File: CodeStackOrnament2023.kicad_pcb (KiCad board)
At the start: 2 copper layers, 28 parts, among them SW1 SW_SPST, U1 TLC555xD, U2 74VHC4040FT

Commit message: starting board design
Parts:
- removed C8: 10uf, Capacitor_SMD:C_0805_2012Metric
- removed the D1 at (117.3, 92.1)
- removed R3: 0, Resistor_SMD:R_0805_2012Metric
- added D1: LED_Small, CodeStackOrnament2023Footprints:156120RS75300_LED, F.Cu at (178.2, 89.0)
- added D1: LED_Small, CodeStackOrnament2023Footprints:156120RS75300_LED, F.Cu at (182.2, 105.1)
- added D1: LED_Small, CodeStackOrnament2023Footprints:156120RS75300_LED, F.Cu at (165.6, 132.8)
- added D1: LED_Small, CodeStackOrnament2023Footprints:156120RS75300_LED, F.Cu at (134.4, 76.4)
- added D1: LED_Small, CodeStackOrnament2023Footprints:156120RS75300_LED, F.Cu at (149.5, 136.8)
- added D1: LED_Small, CodeStackOrnament2023Footprints:156120RS75300_LED, F.Cu at (150.5, 72.4)
- added D1: LED_Small, CodeStackOrnament2023Footprints:156120RS75300_LED, F.Cu at (122.4, 88.0)
- added D1: LED_Small, CodeStackOrnament2023Footprints:156120RS75300_LED, F.Cu at (121.8, 120.2)
- added D1: LED_Small, CodeStackOrnament2023Footprints:156120RS75300_LED, F.Cu at (117.8, 104.1)
- added D1: LED_Small, CodeStackOrnament2023Footprints:156120RS75300_LED, F.Cu at (166.6, 77.0)
- added D1: LED_Small, CodeStackOrnament2023Footprints:156120RS75300_LED, F.Cu at (133.4, 132.2)
- added D1: LED_Small, CodeStackOrnament2023Footprints:156120RS75300_LED, F.Cu at (177.6, 121.2)
- BT1: footprint CodeStackOrnament2023Footprints:2466_AAA_HOLDER -> CodeStackOrnament2023Footprints:BAT_2468
- C1: value c=C_Polarized_Small -> 10uF
- C5: value 0.01uF -> 0.1u
- C7: value 0.1u -> 10uf
- R1, R2: value R -> 8k
- U1: footprint Package_SO:SOIC-8_3.9x4.9mm_P1.27mm -> CodeStackOrnament2023Footprints:TLC555_SOIC
- moved C1 135.7 mm to (247.6, 71.6)
- moved C2 135.7 mm to (247.6, 74.6)
- moved C3 135.7 mm to (247.6, 77.6)
- moved C4 135.7 mm to (247.6, 80.6)
- moved C5 135.7 mm to (247.6, 83.7)
- moved C6 135.7 mm to (247.6, 86.7)
- moved C7 135.7 mm to (247.6, 89.7)
- moved D11 114.3 mm to (213.0, 20.8)
- moved D2 108.8 mm to (211.5, 40.7)
- moved D3 108.8 mm to (211.5, 43.8)
- moved D4 108.8 mm to (211.5, 46.9)
- moved D10 106.5 mm to (212.1, 28.5)
- moved D5 97.9 mm to (211.5, 50.0)
- moved D7 97.9 mm to (211.5, 56.2)
- moved D6 97.9 mm to (211.5, 53.1)
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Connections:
- SW1 pad 1: Net-(BT1-+) -> (no net)
- SW1 pad 2: Net-(SW1-B) -> Net-(BT1-+)
- SW1 pad 3: (no net) -> Net-(SW1-B)
- U2 pad 10: Net-(U2-CLK) -> Net-(U1-Q)
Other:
- board outline added: 68.8 x 68.8 mm

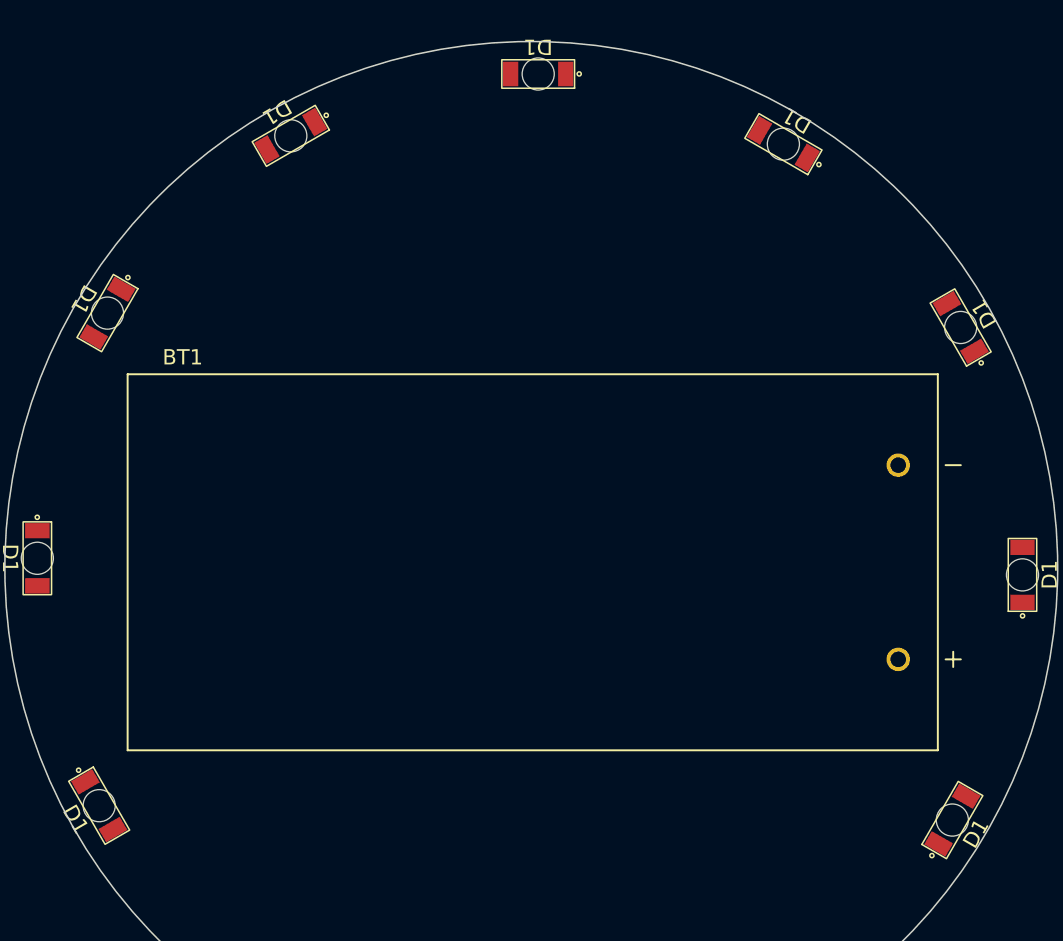
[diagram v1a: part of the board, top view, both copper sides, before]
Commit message: updating footprints
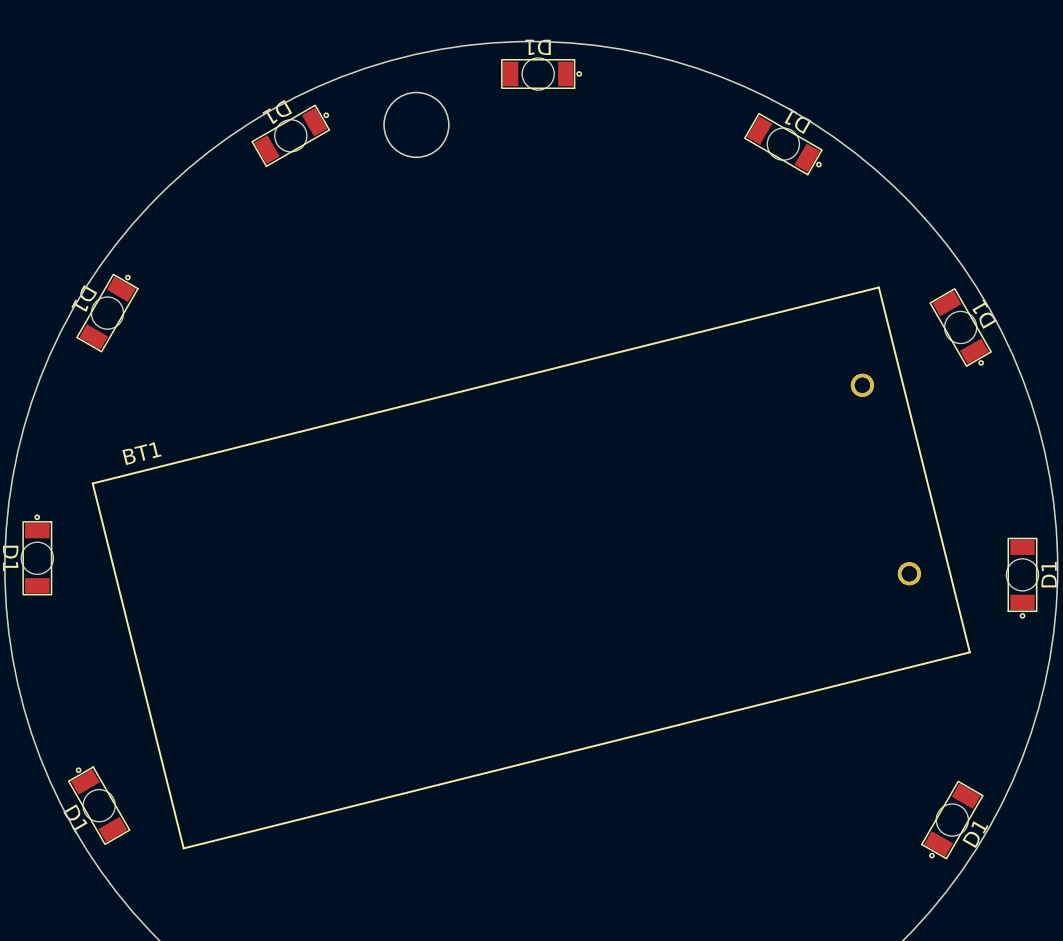
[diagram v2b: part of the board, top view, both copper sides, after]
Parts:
- moved BT1 0.38 mm to (150.1, 104.7), turned to 14 degrees
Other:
- outline, holes or cut-outs redrawn
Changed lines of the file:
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@@
+    )
+  )
+  (footprint "CodeStackOrnament2023Footprints:BAT_2468" (layer "F.Cu")
+    (at 150.09 104.688605 14)
+    (property "Sheetfile" "CodeStackOrnament2023.kicad_sch")
+    (property "Sheetname" "")
+    (property "Sim.Device" "V")
+    (property "Sim.Params" "dc=\"\"")
+    (property "Sim.Pins" "1=+ 2=-")
+    (property "Sim.Type" "DC")
+    (property "ki_description" "Single-cell battery")
+    (property "ki_keywords" "battery cell")
+    (attr through_hole)
+    (fp_text reference "BT1" (at -22.89 -13.4 14) (layer "F.SilkS")
+        (effects (font (size 1 1) (thickness 0.15)))
+    )
+    (fp_text value "Battery_Cell" (at -20.985 13.4 14) (layer "F.Fab")
+        (effects (font (size 1 1) (thickness 0.15)))
+    )
+    (fp_line (start -26.49 -12.295) (end 26.49 -12.295)
+      (stroke (width 0.127) (type solid)) (layer "F.SilkS"))
+    (fp_line (start -26.49 12.295) (end -26.49 -12.295)
+      (stroke (width 0.127) (type solid)) (layer "F.SilkS"))
+    (fp_line (start 26.49 -12.295) (end 26.49 12.295)
+      (stroke (width 0.127) (type solid)) (layer "F.SilkS"))
+    (fp_line (start 26.49 12.295) (end -26.49 12.295)
+      (stroke (width 0.127) (type solid)) (layer "F.SilkS"))
+    (fp_line (start -26.74 -12.545) (end 26.74 -12.545)
+      (stroke (width 0.05) (type solid)) (layer "F.CrtYd"))
+    (fp_line (start -26.74 12.545) (end -26.74 -12.545)
+      (stroke (width 0.05) (type solid)) (layer "F.CrtYd"))
+    (fp_line (start 26.74 -12.545) (end 26.74 12.545)
+      (stroke (width 0.05) (type solid)) (layer "F.CrtYd"))
+    (fp_line (start 26.74 12.545) (end -26.74 12.545)
+      (stroke (width 0.05) (type solid)) (layer "F.CrtYd"))
+    (fp_line (start -26.49 -12.295) (end 26.49 -12.295)
+      (stroke (width 0.127) (type solid)) (layer "F.Fab"))
+    (fp_line (start -26.49 12.295) (end -26.49 -12.295)
+      (stroke (width 0.127) (type solid)) (layer "F.Fab"))
+    (fp_line (start 26.49 -12.295) (end 26.49 12.295)
+      (stroke (width 0.127) (type solid)) (layer "F.Fab"))
+    (fp_line (start 26.49 12.295) (end -26.49 12.295)
+      (stroke (width 0.127) (type solid)) (layer "F.Fab"))
+    (pad "1" thru_hole circle (at 23.9 6.35 14) (size 1.53 1.53) (drill 1.02) (layers "*.Cu" "*.Mask")
+      (net 1 "Net-(BT1-+)") (pinfunction "+") (pintype "passive") (solder_mask_margin 0.102))
+    (pad "2" thru_hole circle (at 23.9 -6.35 14) (size 1.53 1.53) (drill 1.02) (layers "*.Cu" "*.Mask")
+      (net 2 "GND") (pinfunction "-") (pintype "passive") (solder_mask_margin 0.102))
+    (model "${KIPRJMOD}/lib/2468.step"
+      (offset (xyz -6.5 -1.5 10))
+      (scale (xyz 1 1 1))
+      (rotate (xyz -90 0 0))
     )
   )
@@
     )
   )
-  (footprint "CodeStackOrnament2023Footprints:BAT_2468" (layer "F.Cu")
-    (at 150.184645 104.318605)
-    (property "Sheetfile" "CodeStackOrnament2023.kicad_sch")
-    (property "Sheetname" "")
-    (property "Sim.Device" "V")
-    (property "Sim.Params" "dc=\"\"")
-    (property "Sim.Pins" "1=+ 2=-")
-    (property "Sim.Type" "DC")
-    (property "ki_description" "Single-cell battery")
-    (property "ki_keywords" "battery cell")
-    (attr through_hole)
-    (fp_text reference "BT1" (at -22.89 -13.4) (layer "F.SilkS")
-        (effects (font (size 1 1) (thickness 0.15)))
-    )
-    (fp_text value "Battery_Cell" (at -20.985 13.4) (layer "F.Fab")
-        (effects (font (size 1 1) (thickness 0.15)))
-    )
-    (fp_line (start -26.49 -12.295) (end 26.49 -12.295)
-      (stroke (width 0.127) (type solid)) (layer "F.SilkS"))
-    (fp_line (start -26.49 12.295) (end -26.49 -12.295)
-      (stroke (width 0.127) (type solid)) (layer "F.SilkS"))
-    (fp_line (start 26.49 -12.295) (end 26.49 12.295)
-      (stroke (width 0.127) (type solid)) (layer "F.SilkS"))
-    (fp_line (start 26.49 12.295) (end -26.49 12.295)
-      (stroke (width 0.127) (type solid)) (layer "F.SilkS"))
-    (fp_line (start 26.995 -6.35) (end 27.995 -6.35)
-      (stroke (width 0.127) (type solid)) (layer "F.SilkS"))
-    (fp_line (start 26.995 6.35) (end 27.995 6.35)
-      (stroke (width 0.127) (type solid)) (layer "F.SilkS"))
-    (fp_line (start 27.495 5.85) (end 27.495 6.85)
-      (stroke (width 0.127) (type solid)) (layer "F.SilkS"))
-    (fp_line (start -26.74 -12.545) (end 26.74 -12.545)
-      (stroke (width 0.05) (type solid)) (layer "F.CrtYd"))
-    (fp_line (start -26.74 12.545) (end -26.74 -12.545)
-      (stroke (width 0.05) (type solid)) (layer "F.CrtYd"))
-    (fp_line (start 26.74 -12.545) (end 26.74 12.545)
-      (stroke (width 0.05) (type solid)) (layer "F.CrtYd"))
-    (fp_line (start 26.74 12.545) (end -26.74 12.545)
-      (stroke (width 0.05) (type solid)) (layer "F.CrtYd"))
-    (fp_line (start -26.49 -12.295) (end 26.49 -12.295)
-      (stroke (width 0.127) (type solid)) (layer "F.Fab"))
-    (fp_line (start -26.49 12.295) (end -26.49 -12.295)
-      (stroke (width 0.127) (type solid)) (layer "F.Fab"))
-    (fp_line (start 26.49 -12.295) (end 26.49 12.295)
-      (stroke (width 0.127) (type solid)) (layer "F.Fab"))
-    (fp_line (start 26.49 12.295) (end -26.49 12.295)
-      (stroke (width 0.127) (type solid)) (layer "F.Fab"))
-    (fp_line (start 26.995 -6.35) (end 27.995 -6.35)
-      (stroke (width 0.127) (type solid)) (layer "F.Fab"))
-    (fp_line (start 26.995 6.35) (end 27.995 6.35)
-      (stroke (width 0.127) (type solid)) (layer "F.Fab"))
-    (fp_line (start 27.495 5.85) (end 27.495 6.85)
-      (stroke (width 0.127) (type solid)) (layer "F.Fab"))
-    (pad "1" thru_hole circle (at 23.9 6.35) (size 1.53 1.53) (drill 1.02) (layers "*.Cu" "*.Mask")
-      (net 1 "Net-(BT1-+)") (pinfunction "+") (pintype "passive") (solder_mask_margin 0.102))
-    (pad "2" thru_hole circle (at 23.9 -6.35) (size 1.53 1.53) (drill 1.02) (layers "*.Cu" "*.Mask")
-      (net 2 "GND") (pinfunction "-") (pintype "passive") (solder_mask_margin 0.102))
-    (model "${KIPRJMOD}/lib/2468.step"
-      (offset (xyz -6.5 -1.5 10))
-      (scale (xyz 1 1 1))
-      (rotate (xyz -90 0 0))
-    )
-  )
   (footprint "CodeStackOrnament2023Footprints:156120RS75300_LED" (layer "F.Cu")
     (at 134.36502 76.433956 -150)
@@
     )
   )
+  (gr_circle (center 142.58 75.72) (end 144.59 76.39)
+    (stroke (width 0.1) (type default)) (fill none) (layer "Edge.Cuts"))
   (gr_circle (center 150.09 104.688605) (end 170.99 132.038605)
     (stroke (width 0.1) (type default)) (fill none) (layer "Edge.Cuts"))

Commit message: board layout
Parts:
- F1: footprint Resistor_SMD:R_0805_2012Metric -> CodeStackOrnament2023Footprints:SMD1206B050TF_FUSE
- moved C2 115.9 mm to (144.3, 127.3), turned to 90 degrees
- moved C1 115.6 mm to (144.4, 123.7), turned to 90 degrees
- moved C5 112.7 mm to (141.2, 120.8)
- moved C3 112.2 mm to (148.0, 129.3)
- moved C4 107.4 mm to (151.8, 129.3), turned to 180 degrees
- moved U2 99.1 mm to (137.4, 124.9)
- moved C7 96.3 mm to (158.1, 125.3), turned to -90 degrees
- moved C6 95.5 mm to (160.3, 125.3), turned to -90 degrees
- moved U1 81.7 mm to (147.4, 123.3)
- moved SW1 62.1 mm to (166.0, 124.3), turned to -90 degrees
- moved R2 60.9 mm to (154.9, 127.0), turned to -90 degrees
- moved R1 60.5 mm to (154.9, 123.3), turned to -90 degrees
- moved F1 33.1 mm to (178.9, 106.1), turned to 90 degrees
- moved D1 7.88 mm to (127.2, 81.8), turned to -134 degrees
- moved D1 7.88 mm to (141.7, 73.5), turned to -164 degrees
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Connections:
- F1 pad 1: +3V0 -> Net-(SW1-A)
- F1 pad 2: Net-(SW1-B) -> Net-(BT1-+)
- SW1 pad 2: Net-(BT1-+) -> Net-(SW1-A)
- SW1 pad 3: Net-(SW1-B) -> +3V0
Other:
- outline, holes or cut-outs redrawn

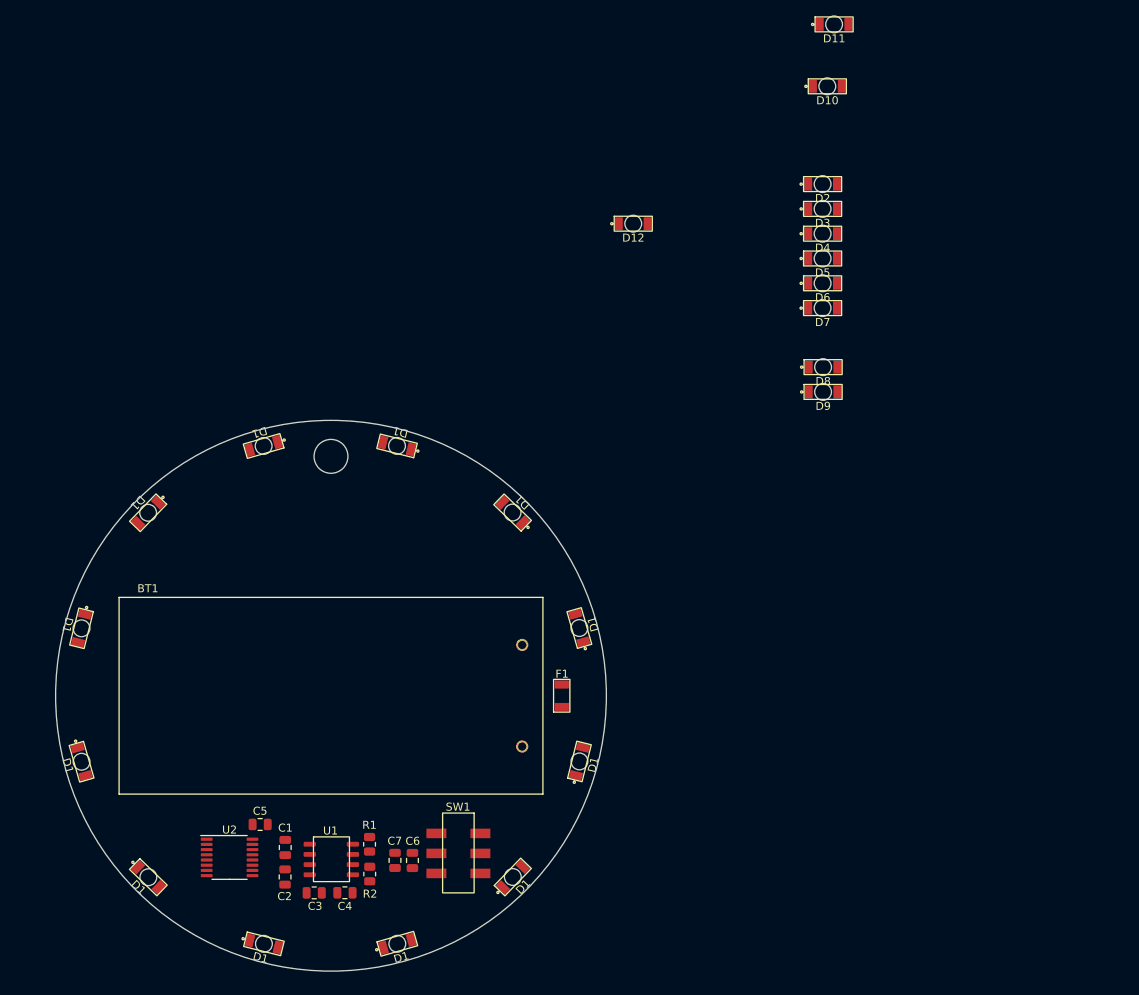
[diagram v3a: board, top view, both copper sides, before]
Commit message: starting board routing
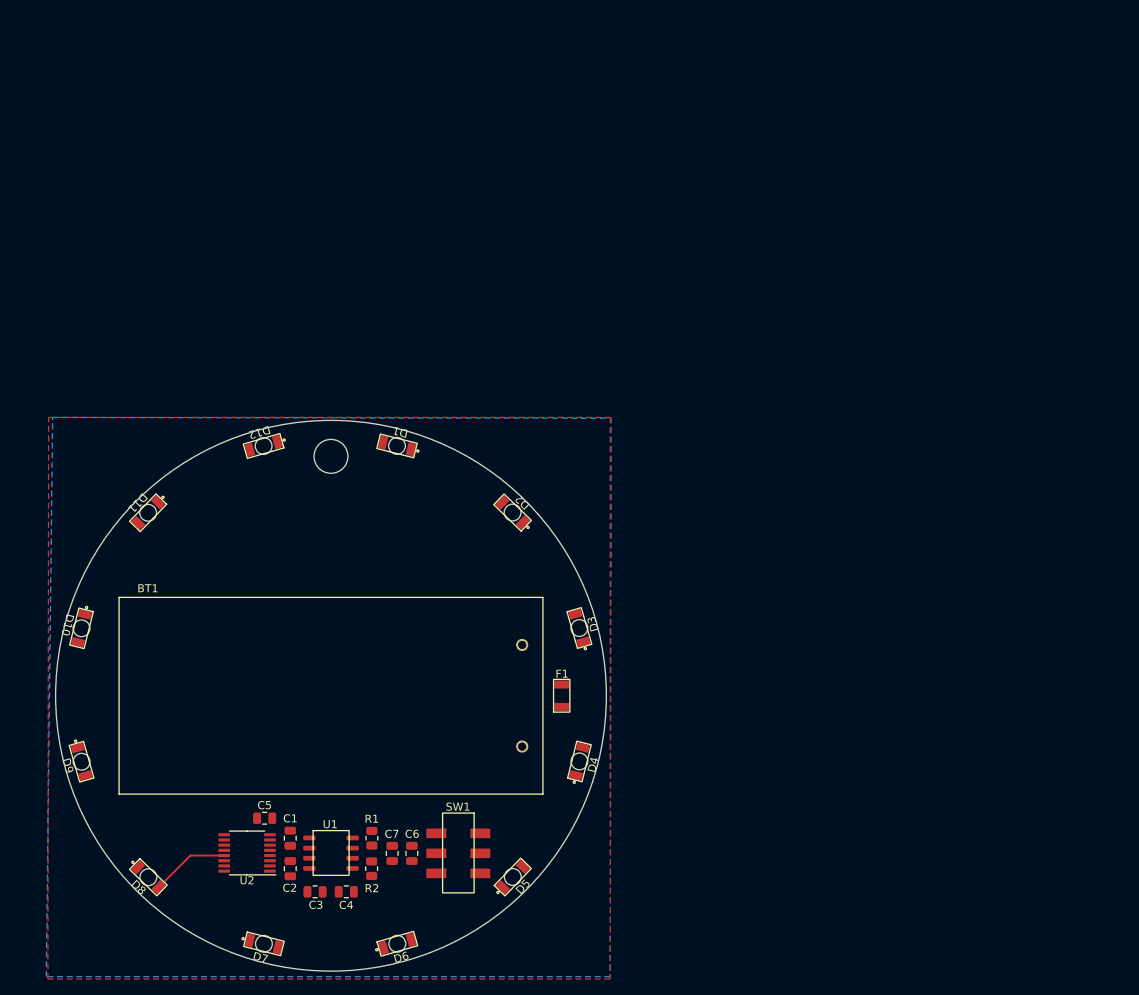
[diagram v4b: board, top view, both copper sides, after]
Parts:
- removed the D10 at (212.1, 28.5)
- removed the D11 at (213.0, 20.8)
- removed the D12 at (187.9, 45.7)
- removed the D2 at (211.5, 40.7)
- removed the D3 at (211.5, 43.8)
- removed the D4 at (211.5, 46.9)
- removed the D5 at (211.5, 50.0)
- removed the D6 at (211.5, 53.1)
- removed the D7 at (211.5, 56.2)
- removed the D8 at (211.6, 63.6)
- removed the D9 at (211.6, 66.7)
- moved U2 2.26 mm to (139.6, 124.3), turned to 180 degrees
- moved C1 1.32 mm to (145.0, 122.5)
- moved C2 1.23 mm to (145.0, 126.3)
- moved C5 0.97 mm to (141.8, 120.0), turned to 180 degrees
- moved C7 0.94 mm to (157.7, 124.4)
- moved C6 0.88 mm to (160.2, 124.4)
- moved R1 0.81 mm to (155.2, 122.5)
- moved U1 0.79 mm to (147.4, 122.5)
- moved R2 0.72 mm to (155.2, 126.3)
- moved C4 0.21 mm to (152.0, 129.2)
- moved C3 0.17 mm to (148.1, 129.2)
- renumbered D1 to D10, D1 to D11, D1 to D12, D1 to D2, D1 to D3, D1 to D4, D1 to D5, D1 to D6, D1 to D7, D1 to D8, D1 to D9
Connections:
- D10 pad 2: Net-(D1-A) -> Net-(D10-A)
- D11 pad 2: Net-(D1-A) -> Net-(D11-A)
- D12 pad 2: Net-(D1-A) -> Net-(D12-A)
- D2 pad 2: Net-(D1-A) -> Net-(D2-A)
- D3 pad 2: Net-(D1-A) -> Net-(D3-A)
- D4 pad 2: Net-(D1-A) -> Net-(D4-A)
- D5 pad 2: Net-(D1-A) -> Net-(D5-A)
- D6 pad 2: Net-(D1-A) -> Net-(D6-A)
- D7 pad 2: Net-(D1-A) -> Net-(D7-A)
- D8 pad 2: Net-(D1-A) -> Net-(D8-A)
- D9 pad 2: Net-(D1-A) -> Net-(D9-A)
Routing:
- net Net-(D8-A): track 0.00 -> 9.82 mm
- added copper zone on B.Cu, net GND
- added copper zone on F.Cu, net GND

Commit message: more routing
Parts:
- U2: footprint Package_SO:TSSOP-16_4.4x5mm_P0.65mm -> CodeStackOrnament2023Footprints:CD74HC4040M96_SOIC16
- moved C5 10.8 mm to (139.2, 130.5), turned to 0 degrees
- moved U2 4.61 mm to (141.9, 128.3), turned to 90 degrees
- moved C1 0.10 mm to (145.1, 122.5)
- turned SW1 to 90 degrees
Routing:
- net +3V0: track 0.00 -> 117.9 mm
- net Net-(D11-A): track 0.00 -> 66.5 mm
- net Net-(D12-A): track 0.00 -> 61.6 mm
- net Net-(D4-A): track 0.00 -> 54.9 mm
- net Net-(D1-A): track 0.00 -> 54.7 mm
- net Net-(D2-A): track 0.00 -> 54.6 mm
- net Net-(D3-A): track 0.00 -> 52.3 mm
- net Net-(D10-A): track 0.00 -> 47.9 mm
- net Net-(D5-A): track 0.00 -> 38.8 mm
- net Net-(SW1-A): track 0.00 -> 23.8 mm
- net Net-(D6-A): track 0.00 -> 22.1 mm
- net Net-(D9-A): track 0.00 -> 21.4 mm
- net Net-(D7-A): track 0.00 -> 15.3 mm
- net Net-(U1-Q): track 0.00 -> 12.0 mm
- net Net-(U1-THR): track 0.00 -> 11.8 mm
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
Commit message: more routing and layout
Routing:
- net GND: track 0.00 -> 91.4 mm

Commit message: Finishing routing.
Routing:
- net GND: track 91.4 -> 103.8 mm, vias 0 -> 10
- net Net-(D2-A): track 54.6 -> 58.7 mm
- net Net-(D3-A): track 52.3 -> 53.3 mm
- net Net-(D9-A): track 21.4 -> 22.0 mm
- net Net-(D12-A): track 61.6 -> 62.2 mm
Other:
- board text added: "OFF"
- board text added: "ON"
